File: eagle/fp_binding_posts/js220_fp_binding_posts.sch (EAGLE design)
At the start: 10 parts, among them J1 111-0703-001, J2 111-0702-001, J3 111-0703-001, J4 111-0702-001, J5 TSM-105-01-S-SV

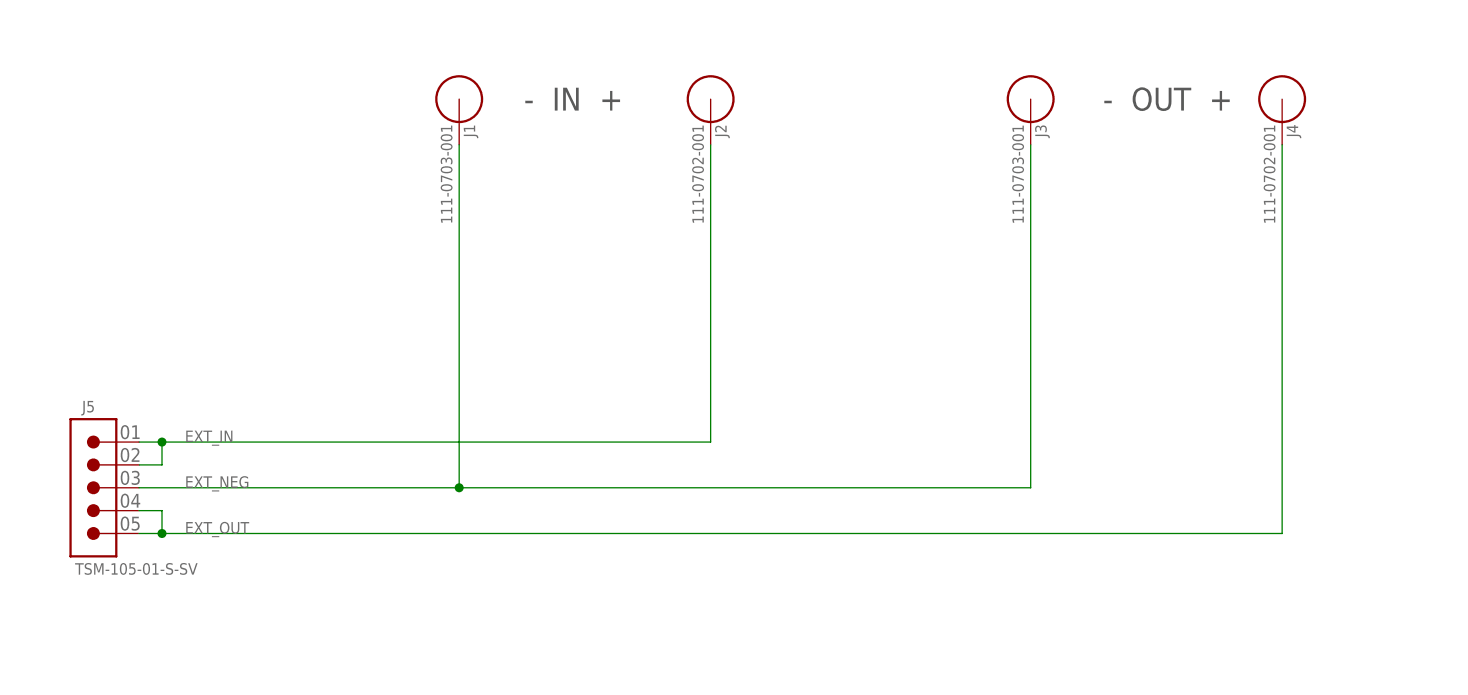
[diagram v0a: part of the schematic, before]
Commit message: Completed revA for the initial end panels.
* Binding post front panel.
* Back panel.
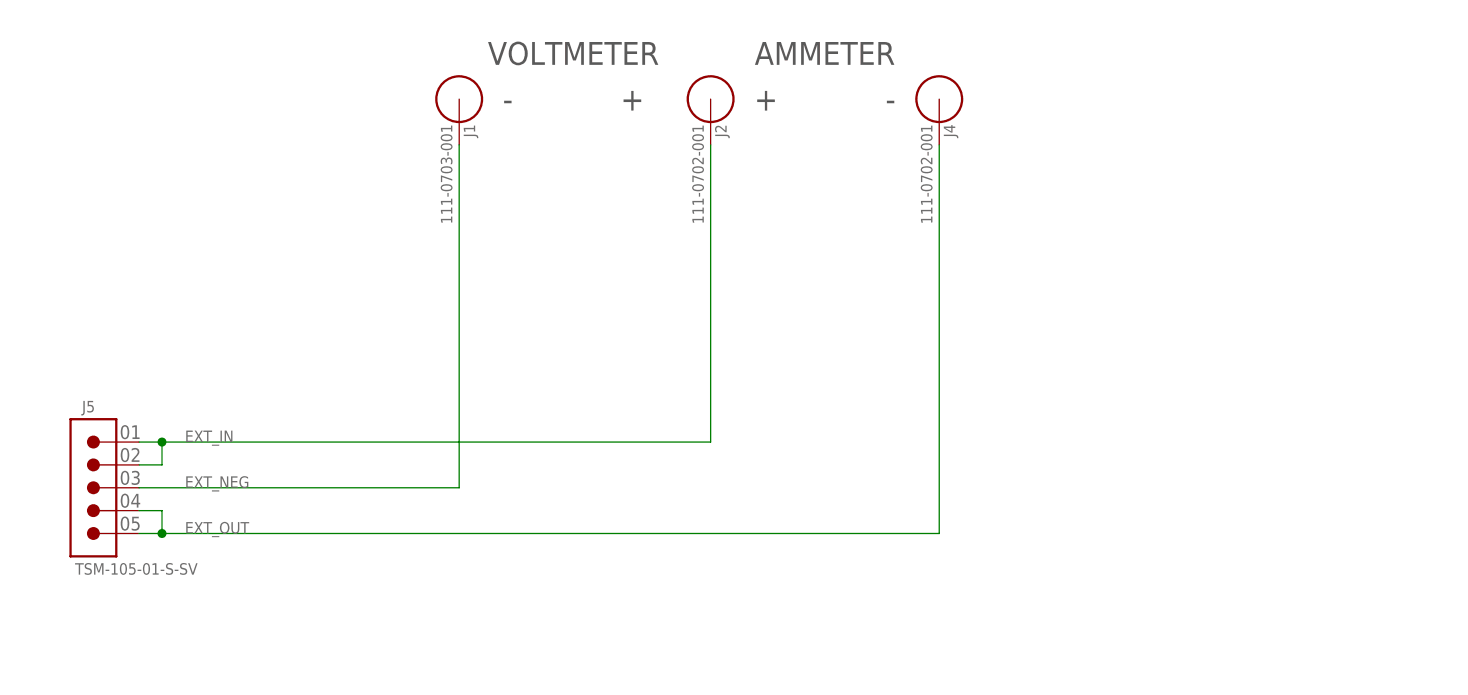
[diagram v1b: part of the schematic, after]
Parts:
- removed J3: 111-0703-001, jetperch:BINDING_POST_6
- H2, H3: value HOLE_#6 -> HOLE_#6_NORESTRICT; device jetperch:HOLE_#6 -> jetperch:HOLE_#6_NORESTRICT
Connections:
- net EXT_NEG: no longer J3.1
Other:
- note added: "+ -"
- note added: "- +"
- note added: "AMMETER"
- note added: "VOLTMETER"
- note removed: "- IN +"
- note removed: "- OUT +"
- moved on the sheet: J4

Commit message: Updated for p3
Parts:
- added J3: 111-0702-001, jetperch:BINDING_POST_6
- J1: MPN (none) -> 111-0703-001
- J2: MPN (none) -> 111-0702-001
- J4: value 111-0702-001 -> 111-0707-001; MPN (none) -> 111-0707-001
- J5: value TSM-105-01-S-SV -> TSM-105-01-L-SV-A; device jetperch:CONN_0.1_5X1_MSA -> jetperch:CONN_0.1_3X2_MSA; MPN TSM-105-01-S-SV -> TSM-105-01-L-SV-A
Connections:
- removed net EXT_IN: J2.1, J5.1, J5.2
- removed net EXT_NEG: J1.1, J5.3
- removed net EXT_OUT: J4.1, J5.4, J5.5
- new net I+: J3.1, J5.1, J5.2
- new net I-: J4.1, J5.3, J5.4
- new net V+: J2.1, J5.6
- new net V-: J1.1, J5.5
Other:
- note added: "C"
- note removed: "B"
- moved on the sheet: J1, J2, J4

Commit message: Updated to rev B.
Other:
- note added: "B"
- note removed: "C"
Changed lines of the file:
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@@
 <plain>
 <text x="177.8" y="26.162" size="5.08" layer="97">Front Panel - Binding Posts</text>
-<text x="266.7" y="6.35" size="3.175" layer="97">C</text>
+<text x="266.7" y="6.35" size="3.175" layer="97">B</text>
 <text x="144.78" y="198.12" size="2.54" layer="97" align="center">+            -</text>
 <text x="144.78" y="203.2" size="2.54" layer="97" align="center">AMMETER</text>

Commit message: Updated for JS220 p3.
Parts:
- removed H3: HOLE_#6_NORESTRICT, jetperch:HOLE_#6_NORESTRICT
- added H1: HOLE_#6_NORESTRICT, jetperch:HOLE_#6_NORESTRICT
- H2: POPULATE (none) -> 0
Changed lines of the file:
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@@
 <part name="FUD2" library="jetperch" deviceset="FIDUCIAL" device="_1MM"/>
 <part name="FUD3" library="jetperch" deviceset="FIDUCIAL" device="_1MM"/>
-<part name="H2" library="jetperch" deviceset="HOLE" device="_#6_NORESTRICT" value="HOLE_#6_NORESTRICT"/>
-<part name="H3" library="jetperch" deviceset="HOLE" device="_#6_NORESTRICT" value="HOLE_#6_NORESTRICT"/>
+<part name="H1" library="jetperch" deviceset="HOLE" device="_#6_NORESTRICT" value="HOLE_#6_NORESTRICT">
+<attribute name="POPULATE" value="0"/>
+</part>
+<part name="H2" library="jetperch" deviceset="HOLE" device="_#6_NORESTRICT" value="HOLE_#6_NORESTRICT">
+<attribute name="POPULATE" value="0"/>
+</part>
 <part name="J2" library="jetperch" deviceset="BINDING_POST" device="_6" value="111-0702-001">
 <attribute name="MPN" value="111-0702-001"/>
+<attribute name="POPULATE" value="1"/>
+</part>
+<part name="PCB1" library="jetperch" deviceset="PCB" device="" value="JS220_fp_bp_pcb_revB">
+<attribute name="MPN" value="JS220_fp_bp_pcb_revB"/>
 <attribute name="POPULATE" value="1"/>
 </part>
@@
 <instance part="FUD2" gate="G$1" x="12.7" y="205.74" smashed="yes"/>
 <instance part="FUD3" gate="G$1" x="17.78" y="205.74" smashed="yes"/>
-<instance part="H2" gate="G$1" x="7.62" y="200.66" smashed="yes"/>
-<instance part="H3" gate="G$1" x="12.7" y="200.66" smashed="yes"/>
+<instance part="H1" gate="G$1" x="7.62" y="200.66" smashed="yes">
+<attribute name="POPULATE" x="7.62" y="200.66" size="1.778" layer="96" display="off"/>
+</instance>
+<instance part="H2" gate="G$1" x="12.7" y="200.66" smashed="yes">
+<attribute name="POPULATE" x="12.7" y="200.66" size="1.778" layer="96" display="off"/>
+</instance>
 <instance part="J2" gate="G$1" x="106.68" y="198.12" smashed="yes" rot="R270">
 <attribute name="MPN" x="106.68" y="198.12" size="1.778" layer="96" display="off"/>
@@
 <attribute name="VALUE" x="104.648" y="195.326" size="1.27" layer="96" rot="R270"/>
 </instance>
+<instance part="PCB1" gate="G$1" x="12.7" y="193.04" smashed="yes">
+<attribute name="VALUE" x="7.62" y="187.96" size="1.27" layer="96"/>
+<attribute name="NAME" x="7.62" y="196.088" size="1.27" layer="95"/>
+<attribute name="POPULATE" x="12.7" y="193.04" size="1.27" layer="96" display="off"/>
+<attribute name="MPN" x="12.7" y="193.04" size="1.27" layer="96" display="off"/>
+</instance>
 </instances>

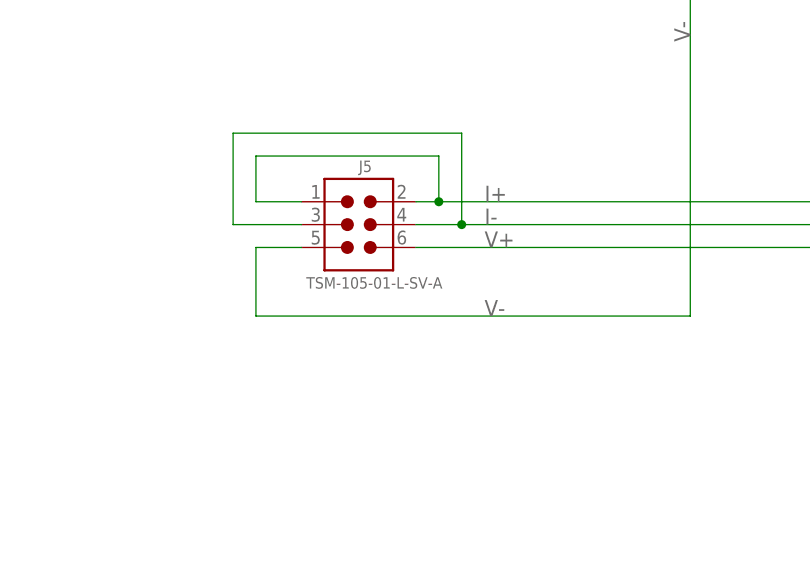
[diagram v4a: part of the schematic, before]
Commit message: Final build files.
Fixed fp_binding_posts with corrected connector.
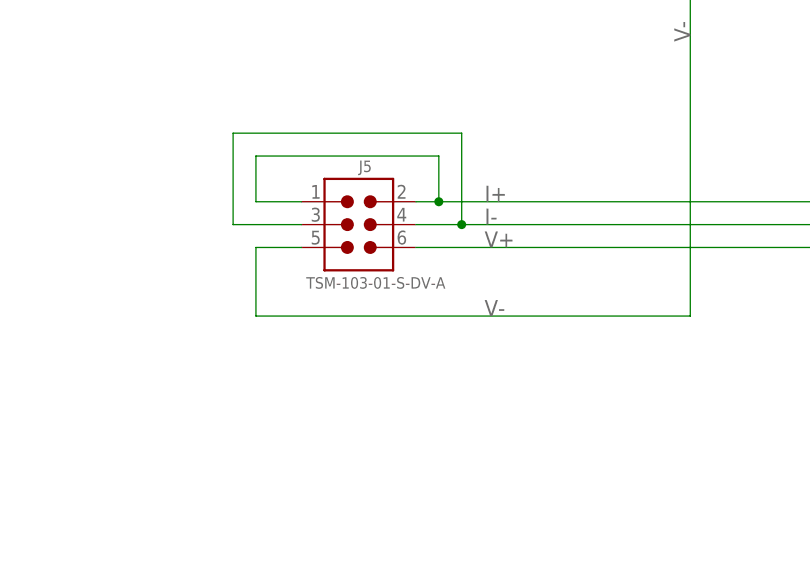
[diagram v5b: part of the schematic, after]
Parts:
- J5: value TSM-105-01-L-SV-A -> TSM-103-01-S-DV-A; MPN TSM-105-01-L-SV-A -> TSM-103-01-S-DV-A
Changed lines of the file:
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@@
 <parts>
 <part name="FRAME1" library="frames" library_urn="urn:adsk.eagle:library:229" deviceset="FRAME_A_L" device="" value="PG1"/>
-<part name="J5" library="jetperch" deviceset="CONN_0.1_3X2" device="_MSA" value="TSM-105-01-L-SV-A">
-<attribute name="MPN" value="TSM-105-01-L-SV-A"/>
+<part name="J5" library="jetperch" deviceset="CONN_0.1_3X2" device="_MSA" value="TSM-103-01-S-DV-A">
+<attribute name="MPN" value="TSM-103-01-S-DV-A"/>
 <attribute name="POPULATE" value="1"/>
 </part>

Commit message: Updated for beta build.
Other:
- note added: "C"
- note removed: "B"
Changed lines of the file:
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@@
 <attribute name="POPULATE" value="1"/>
 </part>
-<part name="PCB1" library="jetperch" deviceset="PCB" device="" value="JS220_fp_bp_pcb_revB">
-<attribute name="MPN" value="JS220_fp_bp_pcb_revB"/>
+<part name="PCB1" library="jetperch" deviceset="PCB" device="" value="JS220_fp_binding_post_pcb_revC">
 <attribute name="POPULATE" value="1"/>
 </part>
@@
 <plain>
 <text x="177.8" y="26.162" size="5.08" layer="97">Front Panel - Binding Posts</text>
-<text x="266.7" y="6.35" size="3.175" layer="97">B</text>
+<text x="266.7" y="6.35" size="3.175" layer="97">C</text>
 <text x="144.78" y="198.12" size="2.54" layer="97" align="center">+            -</text>
 <text x="144.78" y="203.2" size="2.54" layer="97" align="center">AMMETER</text>
@@
 <attribute name="NAME" x="7.62" y="196.088" size="1.27" layer="95"/>
 <attribute name="POPULATE" x="12.7" y="193.04" size="1.27" layer="96" display="off"/>
-<attribute name="MPN" x="12.7" y="193.04" size="1.27" layer="96" display="off"/>
 </instance>
 </instances>
